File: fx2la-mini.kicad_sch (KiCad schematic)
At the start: 1 part

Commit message: Save
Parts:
- added C1, C2: ~, passive:C_0402, symbol Device:C_Small
- added C10, C11, C12, C3, C4, C5, C6, C7, C9: 0.1u, passive:C_0402, symbol Device:C_Small
- added C13, C8: 4.7u, passive:C_0402, symbol Device:C_Small
- added J1: USB_C_Receptacle_USB2.0, connectors:USB_C_Receptacle_USB4105, symbol Connector:USB_C_Receptacle_USB2.0
- added J2: Conn_02x05_Counter_Clockwise, connectors:2x5_2.54mm_side, symbol Connector_Generic:Conn_02x05_Counter_Clockwise
- added R1, R2, R3, R4, R5, R6: 5.1k, passive:R_0402, symbol Device:R_Small
- added U2: NUF8401MNT4G, dfn:DFN-16-1EP_1.6x4mm_P0.5mm, symbol interface_esd:NUF8401MNT4G
- added U3: MIC5504-3.3YM5, Package_TO_SOT_SMD:SOT-23-5, symbol Regulator_Linear:MIC5504-3.3YM5
- added U4: USBLC6-2SC6, Package_TO_SOT_SMD:SOT-23-6, symbol Power_Protection:USBLC6-2SC6
- added Y1: 24 MHz, crystals:Crystal_4Pin_2.0x1.6mm, symbol Device:Crystal_GND24_Small
- U1: renamed from U?; footprint Package_DFN_QFN:QFN-56-1EP_8x8mm_P0.5mm_EP4.5x5.2mm_ThermalVias_TopTented -> Package_DFN_QFN:QFN-56-1EP_8x8mm_P0.5mm_EP4.5x5.2mm
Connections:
- net PB0: now also U2.16 (1B)
- net PB1: now also U2.15 (2B)
- net PB2: now also U2.14 (3B)
- net PB3: now also U2.13 (4B)
- net PB4: now also U2.12 (5B)
- net PB5: now also U2.11 (6B)
- net PB6: now also U2.10 (7B)
- net PB7: now also U2.9 (8B)
- net GND: now reaches U1.10 (AGND), U1.6 (AGND)
- net GND: now also U1.12 (GND), U1.14 (RESERVED), U1.26 (GND), U1.28 (GND), U1.41 (GND), U1.53 (GND), U1.56 (GND), U1.57 (EP), C1.1, C10.2, C11.2, C12.2, C13.2, C2.1, C3.2, C4.2, C5.2, C6.2, C7.2, C8.2, C9.2, J1.A1 (GND), J1.A12 (GND), J1.B1 (GND), J1.B12 (GND), J1.S1 (SHIELD), J2.6 (Pin_6), R5.2, R6.2, U2.17 (GND), U3.2 (GND), U4.2 (GND), Y1.2, Y1.4
- net +3V3: now reaches U1.11 (VCC), U1.17 (VCC), U1.27 (VCC), U1.32 (VCC), U1.43 (VCC), U1.55 (VCC)
- net +3V3: now also U1.3 (AVCC), U1.7 (AVCC), C10.1, C11.1, C12.1, C13.1, C4.1, C5.1, C6.1, C7.1, C9.1, R1.2, R2.2, R3.2, R4.2, U3.5 (VOUT)
- net SCL: now reaches U1.15 (SCL)
- net SCL: now also R2.1
- net SDA: now reaches U1.16 (SDA)
- net SDA: now also R3.1
- net XIN: now reaches U1.4 (XTALOUT)
- net XIN: now also C1.2, Y1.3
- net RST: now reaches U1.42 (~{RESET})
- net RST: now also C3.1, R4.1
- net WAKEUP: now reaches U1.44 (WAKEUP)
- net WAKEUP: now also R1.1
- net XOUT: now reaches U1.5 (XTALIN)
- net XOUT: now also C2.2, Y1.1
- net DP_P: now reaches U1.8 (D+)
- net DP_P: now also U4.6 (I/O1)
- net DP_N: now reaches U1.9 (D-)
- net DP_N: now also U4.4 (I/O2)
- new net +5V: C8.1, J1.A4 (VBUS), J1.A9 (VBUS), J1.B4 (VBUS), J1.B9 (VBUS), U3.1 (VIN), U3.3 (EN), U4.5 (VBUS)
- new net CC1: J1.A5 (CC1), R5.1
- new net CC2: J1.B5 (CC2), R6.1
- new net D_N: J1.A7 (D-), J1.B7 (D-), U4.3 (I/O2)
- new net D_P: J1.A6 (D+), J1.B6 (D+), U4.1 (I/O1)
- new net PB0_OUT: J2.1 (Pin_1), U2.1 (1A)
- new net PB1_OUT: J2.10 (Pin_10), U2.2 (2A)
- new net PB2_OUT: J2.2 (Pin_2), U2.3 (3A)
- new net PB3_OUT: J2.9 (Pin_9), U2.4 (4A)
- new net PB4_OUT: J2.3 (Pin_3), U2.5 (5A)
- new net PB5_OUT: J2.8 (Pin_8), U2.6 (6A)
- new net PB6_OUT: J2.4 (Pin_4), U2.7 (7A)
- new net PB7_OUT: J2.7 (Pin_7), U2.8 (8A)
- no-connect marks 0 -> 26

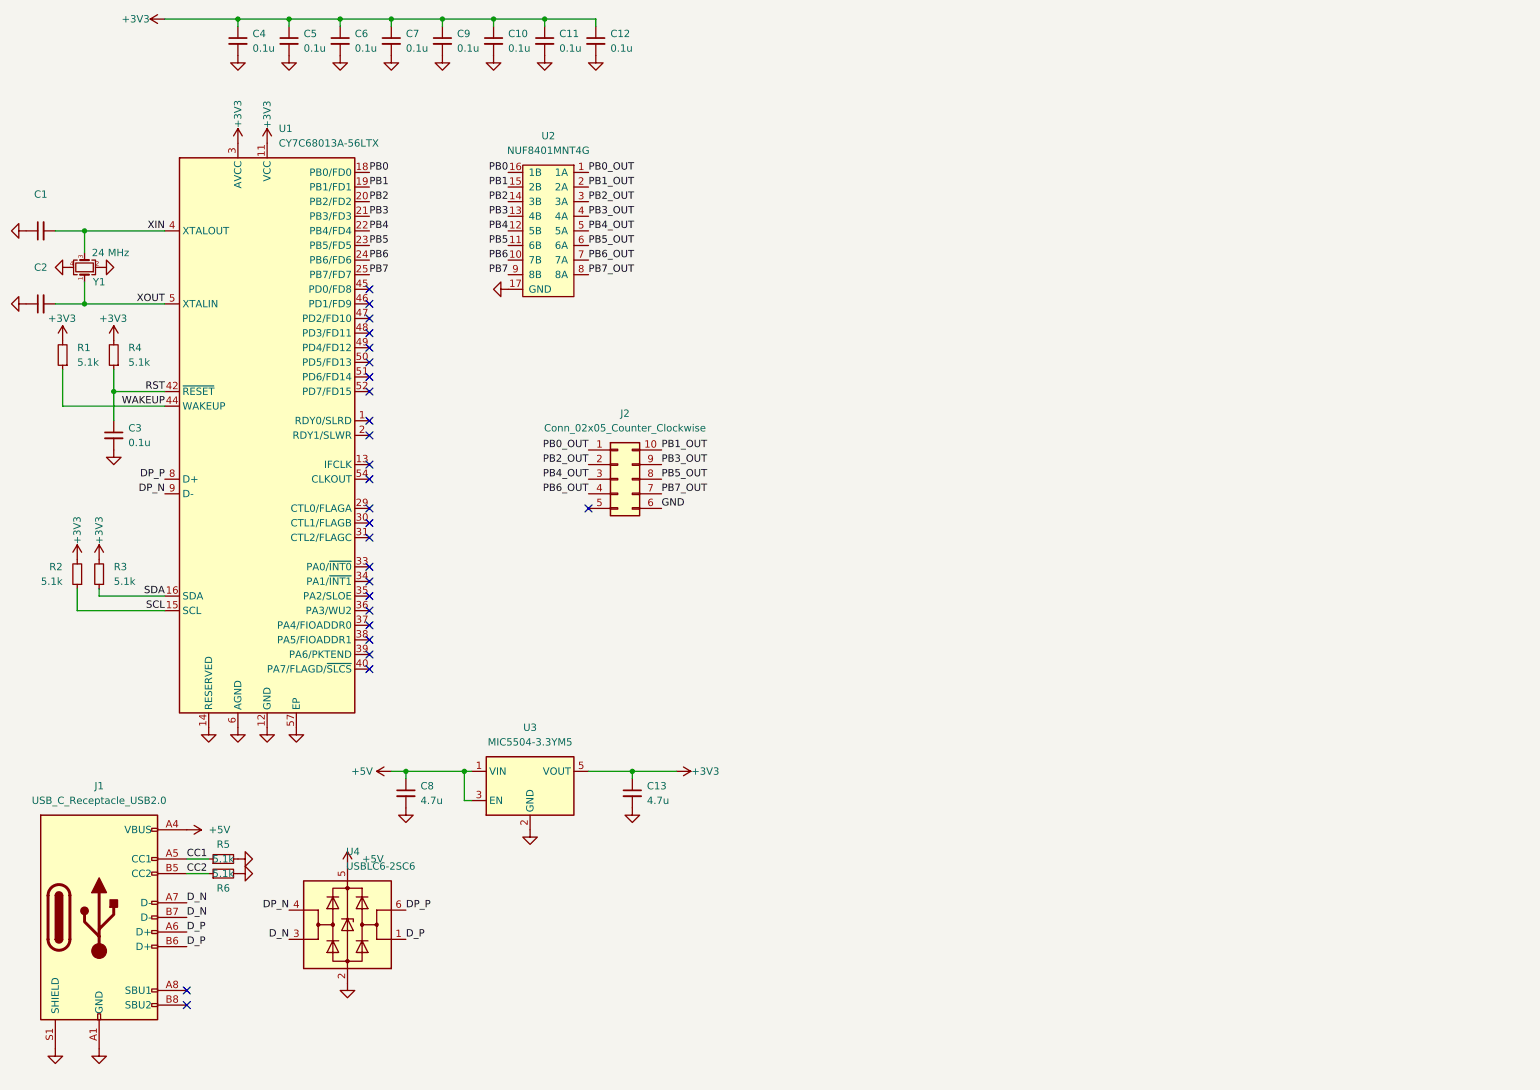
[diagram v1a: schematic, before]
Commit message: Hijack project to 16 channels
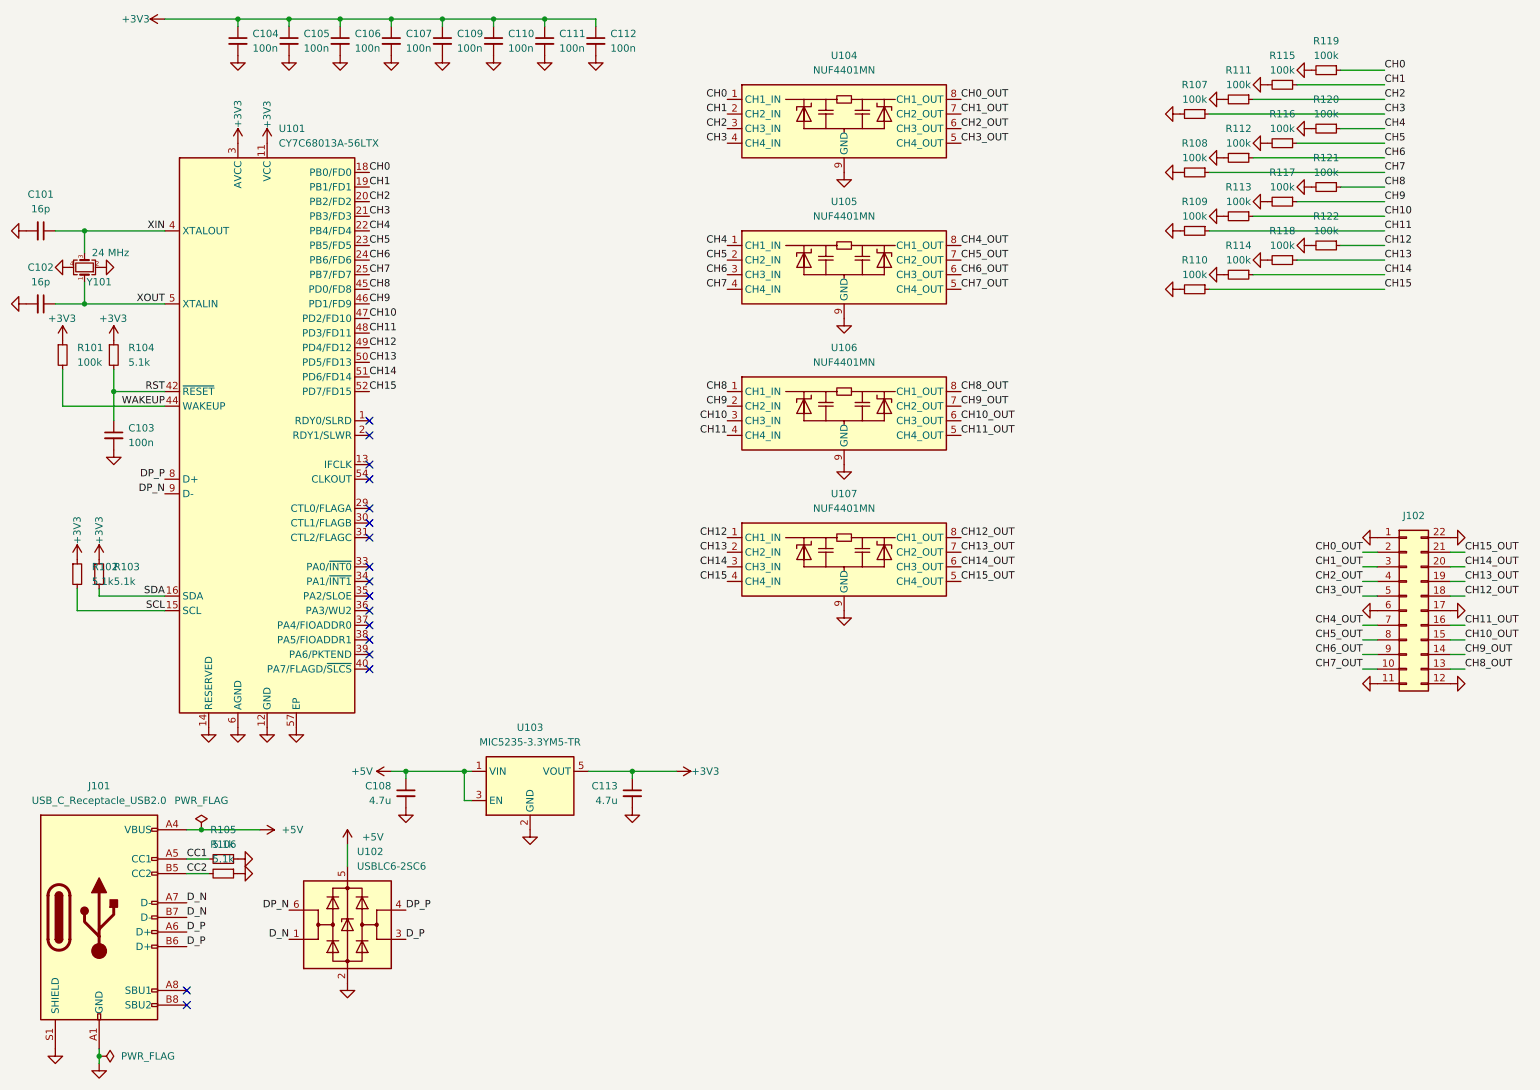
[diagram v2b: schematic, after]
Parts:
- removed C1, C2: ~, passive:C_0402, symbol Device:C_Small
- removed C10, C11, C12, C3, C4, C5, C6, C7, C9: 0.1u, passive:C_0402, symbol Device:C_Small
- removed C13, C8: 4.7u, passive:C_0402, symbol Device:C_Small
- removed J1: USB_C_Receptacle_USB2.0, connectors:USB_C_Receptacle_USB4105, symbol Connector:USB_C_Receptacle_USB2.0
- removed J2: Conn_02x05_Counter_Clockwise, connectors:2x5_2.54mm_side, symbol Connector_Generic:Conn_02x05_Counter_Clockwise
- removed R1, R2, R3, R4, R5, R6: 5.1k, passive:R_0402, symbol Device:R_Small
- removed U2: NUF8401MNT4G, dfn:DFN-16-1EP_1.6x4mm_P0.5mm, symbol interface_esd:NUF8401MNT4G
- removed U4: USBLC6-2SC6, Package_TO_SOT_SMD:SOT-23-6, symbol Power_Protection:USBLC6-2SC6
- added C101, C102: 16p, passive:C_0402, symbol Device:C_Small
- added C103, C104, C105, C106, C107, C109, C110, C111, C112: 100n, passive:C_0402, symbol Device:C_Small
- added C108, C113: 4.7u, passive:C_0402, symbol Device:C_Small
- added J101: USB_C_Receptacle_USB2.0, connectors:USB_C_Receptacle_USB4105, symbol Connector:USB_C_Receptacle_USB2.0
- added J102: Conn_02x11_Counter_Clockwise, connectors:2x11_2.54mm_side, symbol Connector_Generic:Conn_02x11_Counter_Clockwise
- added R101, R107, R108, R109, R110, R111, R112, R113, R114, R115, R116, R117, R118, R119, R120, R121, R122: 100k, passive:R_0402, symbol Device:R_Small
- added R102, R103, R104, R105, R106: 5.1k, passive:R_0402, symbol Device:R_Small
- added U102: USBLC6-2SC6, Package_TO_SOT_SMD:SOT-23-6, symbol Power_Protection:USBLC6-2SC6
- added U104, U105, U106, U107: NUF4401MN, Package_DFN_QFN:DFN-8-1EP_2x2mm_P0.5mm_EP0.7x1.3mm, symbol Power_Protection:NUF4401MN
- U101: renamed from U1; LCSC (none) -> C14912; MFPN (none) -> CY7C68013A-56LTX
- U103: renamed from U3; value MIC5504-3.3YM5 -> MIC5235-3.3YM5-TR; LCSC (none) -> C89886; MFPN (none) -> MIC5235-3.3YM5-TR
- Y101: renamed from Y1; LCSC (none) -> C2689430; MFPN (none) -> E1SB24E000007E
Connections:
- net +3V3: now also C104.1, C105.1, C106.1, C107.1, C109.1, C110.1, C111.1, C112.1, C113.1, R101.1, R102.1, R103.1, R104.1
- net +5V: now also C108.1, J101.A4 (VBUS), J101.A9 (VBUS), J101.B4 (VBUS), J101.B9 (VBUS), U102.5 (VBUS)
- net CC1: now also J101.A5 (CC1), R105.2
- net CC2: now also J101.B5 (CC2), R106.2
- net DP_N: now also U102.6 (I/O1)
- net DP_P: now also U102.4 (I/O2)
- net D_N: now also J101.A7 (D-), J101.B7 (D-), U102.1 (I/O1)
- net D_P: now also J101.A6 (D+), J101.B6 (D+), U102.3 (I/O2)
- net GND: now also C101.2, C102.2, C103.2, C104.2, C105.2, C106.2, C107.2, C108.2, C109.2, C110.2, C111.2, C112.2, C113.2, J101.A1 (GND), J101.A12 (GND), J101.B1 (GND), J101.B12 (GND), J101.S1 (SHIELD), J102.1 (Pin_1), J102.11 (Pin_11), J102.12 (Pin_12), J102.17 (Pin_17), J102.22 (Pin_22), J102.6 (Pin_6), R105.1, R106.1, R107.2, R108.2, R109.2, R110.2, R111.2, R112.2, R113.2, R114.2, R115.2, R116.2, R117.2, R118.2, R119.2, R120.2, R121.2, R122.2, U102.2 (GND), U104.9 (GND), U105.9 (GND), U106.9 (GND), U107.9 (GND)
- net RST: now also C103.1, R104.2
- net SCL: now also R102.2
- net SDA: now also R103.2
- net WAKEUP: now also R101.2
- net XIN: now also C101.1
- net XOUT: now also C102.1
- net CH8: now reaches U101.45 (PD0/FD8)
- net CH8: now also R121.1, U106.1 (CH1_IN)
- net CH9: now reaches U101.46 (PD1/FD9)
- net CH9: now also R117.1, U106.2 (CH2_IN)
- net CH10: now reaches U101.47 (PD2/FD10)
- net CH10: now also R113.1, U106.3 (CH3_IN)
- net CH11: now reaches U101.48 (PD3/FD11)
- net CH11: now also R109.1, U106.4 (CH4_IN)
- net CH12: now reaches U101.49 (PD4/FD12)
- net CH12: now also R122.1, U107.1 (CH1_IN)
- net CH13: now reaches U101.50 (PD5/FD13)
- net CH13: now also R118.1, U107.2 (CH2_IN)
- net CH14: now reaches U101.51 (PD6/FD14)
- net CH14: now also R114.1, U107.3 (CH3_IN)
- net CH15: now reaches U101.52 (PD7/FD15)
- net CH15: now also R110.1, U107.4 (CH4_IN)
- net PB0 renamed CH0
- net CH0: now also R119.1, U104.1 (CH1_IN)
- net PB1 renamed CH1
- net CH1: now also R115.1, U104.2 (CH2_IN)
- net PB2 renamed CH2
- net CH2: now also R111.1, U104.3 (CH3_IN)
- net PB3 renamed CH3
- net CH3: now also R107.1, U104.4 (CH4_IN)
- net PB4 renamed CH4
- net CH4: now also R120.1, U105.1 (CH1_IN)
- net PB5 renamed CH5
- net CH5: now also R116.1, U105.2 (CH2_IN)
- net PB6 renamed CH6
- net CH6: now also R112.1, U105.3 (CH3_IN)
- net PB7 renamed CH7
- net CH7: now also R108.1, U105.4 (CH4_IN)
- new net CH0_OUT: J102.2 (Pin_2), U104.8 (CH1_OUT)
- new net CH10_OUT: J102.15 (Pin_15), U106.6 (CH3_OUT)
- new net CH11_OUT: J102.16 (Pin_16), U106.5 (CH4_OUT)
- new net CH12_OUT: J102.18 (Pin_18), U107.8 (CH1_OUT)
- new net CH13_OUT: J102.19 (Pin_19), U107.7 (CH2_OUT)
- new net CH14_OUT: J102.20 (Pin_20), U107.6 (CH3_OUT)
- new net CH15_OUT: J102.21 (Pin_21), U107.5 (CH4_OUT)
- new net CH1_OUT: J102.3 (Pin_3), U104.7 (CH2_OUT)
- new net CH2_OUT: J102.4 (Pin_4), U104.6 (CH3_OUT)
- new net CH3_OUT: J102.5 (Pin_5), U104.5 (CH4_OUT)
- new net CH4_OUT: J102.7 (Pin_7), U105.8 (CH1_OUT)
- new net CH5_OUT: J102.8 (Pin_8), U105.7 (CH2_OUT)
- new net CH6_OUT: J102.9 (Pin_9), U105.6 (CH3_OUT)
- new net CH7_OUT: J102.10 (Pin_10), U105.5 (CH4_OUT)
- new net CH8_OUT: J102.13 (Pin_13), U106.8 (CH1_OUT)
- new net CH9_OUT: J102.14 (Pin_14), U106.7 (CH2_OUT)
- no-connect marks 26 -> 17

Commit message: Layout complete
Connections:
- net CH0: now also U104.4 (CH4_IN); no longer R119.1, U104.1 (CH1_IN)
- net CH0_OUT: now also R119.1, U104.5 (CH4_OUT); no longer U104.8 (CH1_OUT)
- net CH1: now also U104.3 (CH3_IN); no longer R115.1, U104.2 (CH2_IN)
- net CH10: now also U106.2 (CH2_IN); no longer R113.1, U106.3 (CH3_IN)
- net CH10_OUT: now also R113.1, U106.7 (CH2_OUT); no longer U106.6 (CH3_OUT)
- net CH11: now also U106.1 (CH1_IN); no longer R109.1, U106.4 (CH4_IN)
- net CH11_OUT: now also R109.1, U106.8 (CH1_OUT); no longer U106.5 (CH4_OUT)
- net CH12: now also U107.4 (CH4_IN); no longer R122.1, U107.1 (CH1_IN)
- net CH12_OUT: now also R122.1, U107.5 (CH4_OUT); no longer U107.8 (CH1_OUT)
- net CH13: now also U107.3 (CH3_IN); no longer R118.1, U107.2 (CH2_IN)
- net CH13_OUT: now also R118.1, U107.6 (CH3_OUT); no longer U107.7 (CH2_OUT)
- net CH14: now also U107.2 (CH2_IN); no longer R114.1, U107.3 (CH3_IN)
- net CH14_OUT: now also R114.1, U107.7 (CH2_OUT); no longer U107.6 (CH3_OUT)
- net CH15: now also U107.1 (CH1_IN); no longer R110.1, U107.4 (CH4_IN)
- net CH15_OUT: now also R110.1, U107.8 (CH1_OUT); no longer U107.5 (CH4_OUT)
- net CH1_OUT: now also R115.1, U104.6 (CH3_OUT); no longer U104.7 (CH2_OUT)
- net CH2: now also U104.2 (CH2_IN); no longer R111.1, U104.3 (CH3_IN)
- net CH2_OUT: now also R111.1, U104.7 (CH2_OUT); no longer U104.6 (CH3_OUT)
- net CH3: now also U104.1 (CH1_IN); no longer R107.1, U104.4 (CH4_IN)
- net CH3_OUT: now also R107.1, U104.8 (CH1_OUT); no longer U104.5 (CH4_OUT)
- net CH4: now also U105.4 (CH4_IN); no longer R120.1, U105.1 (CH1_IN)
- net CH4_OUT: now also R120.1, U105.5 (CH4_OUT); no longer U105.8 (CH1_OUT)
- net CH5: now also U105.3 (CH3_IN); no longer R116.1, U105.2 (CH2_IN)
- net CH5_OUT: now also R116.1, U105.6 (CH3_OUT); no longer U105.7 (CH2_OUT)
- net CH6: now also U105.2 (CH2_IN); no longer R112.1, U105.3 (CH3_IN)
- net CH6_OUT: now also R112.1, U105.7 (CH2_OUT); no longer U105.6 (CH3_OUT)
- net CH7: now also U105.1 (CH1_IN); no longer R108.1, U105.4 (CH4_IN)
- net CH7_OUT: now also R108.1, U105.8 (CH1_OUT); no longer U105.5 (CH4_OUT)
- net CH8: now also U106.4 (CH4_IN); no longer R121.1, U106.1 (CH1_IN)
- net CH8_OUT: now also R121.1, U106.5 (CH4_OUT); no longer U106.8 (CH1_OUT)
- net CH9: now also U106.3 (CH3_IN); no longer R117.1, U106.2 (CH2_IN)
- net CH9_OUT: now also R117.1, U106.6 (CH3_OUT); no longer U106.7 (CH2_OUT)
- net DP_N: now also U102.4 (I/O2); no longer U102.6 (I/O1)
- net DP_P: now also U102.6 (I/O1); no longer U102.4 (I/O2)
- net D_N: now also U102.3 (I/O2); no longer U102.1 (I/O1)
- net D_P: now also U102.1 (I/O1); no longer U102.3 (I/O2)
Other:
- moved on the sheet: U104, U105, U106, U107
